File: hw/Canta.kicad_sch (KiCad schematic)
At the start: 41 parts, among them J1 USB_C_Receptacle_PowerOnly_6P, J101 Conn_01x01, J102 Conn_01x01, J103 Conn_01x01, J104 Conn_01x01, J105 Conn_01x01, J106 Conn_01x01, J107 Conn_01x01, J108 Conn_01x01, J109 Conn_01x01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

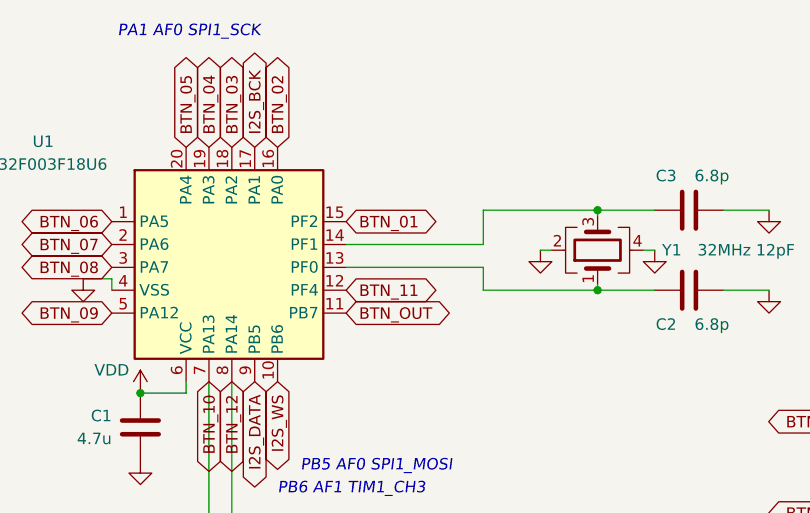
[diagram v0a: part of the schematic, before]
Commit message: Revise pin assignment; submit for fab (Rev. 2)
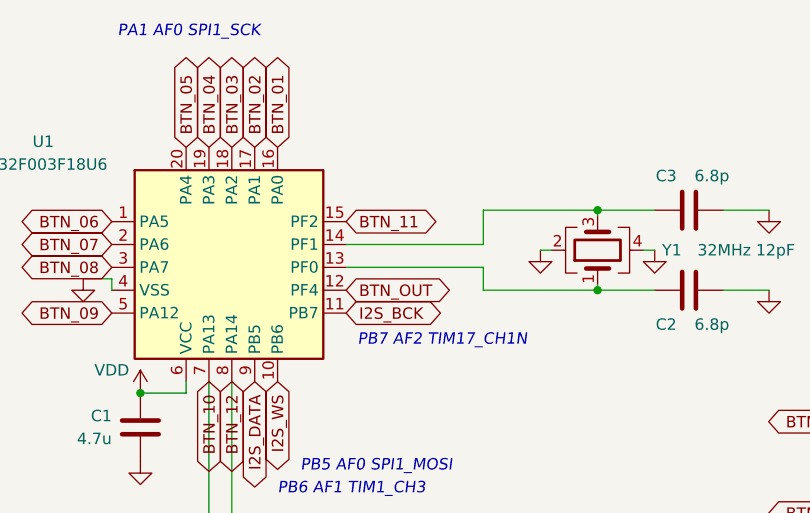
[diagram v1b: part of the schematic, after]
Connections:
- net BTN_01: now also U1.16 (PA0); no longer U1.15 (PF2)
- net BTN_02: now also U1.17 (PA1); no longer U1.16 (PA0)
- net BTN_11: now also U1.15 (PF2); no longer U1.12 (PF4)
- net BTN_OUT: now also U1.12 (PF4); no longer U1.11 (PB7)
- net I2S_BCK: now also U1.11 (PB7); no longer U1.17 (PA1)
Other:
- note added: "PB7 AF2 TIM17_CH1N"

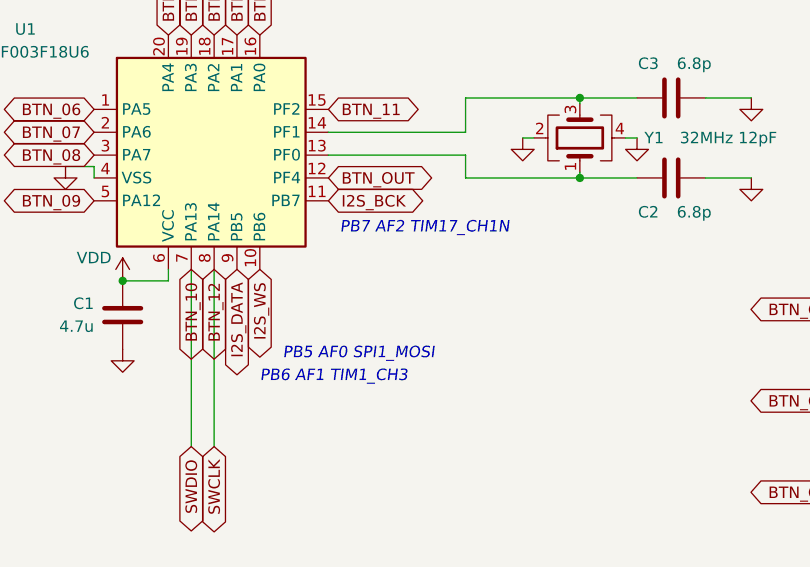
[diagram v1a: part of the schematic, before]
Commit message: Improve signal timings
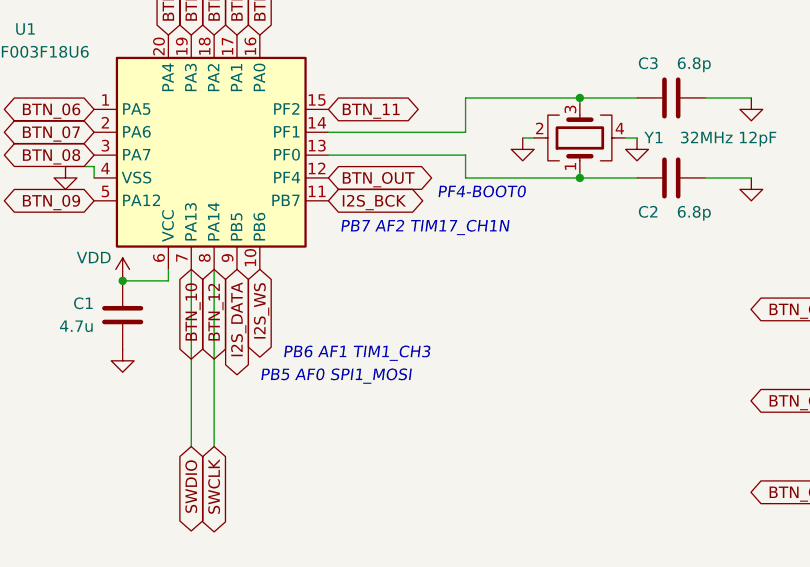
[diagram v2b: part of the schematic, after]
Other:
- note added: "PF4-BOOT0"
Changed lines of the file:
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@@
     (stroke (width 0) (type default))
   )
-  (text "PB5 AF0 SPI1_MOSI" (at 169.545 67.31 0)
+  (text "PB5 AF0 SPI1_MOSI" (at 167.005 69.85 0)
+    (effects (font (size 1.27 1.27) italic) (justify left bottom))
+  )
+  (text "PF4-BOOT0" (at 186.69 49.53 0)
     (effects (font (size 1.27 1.27) italic) (justify left bottom))
   )
@@
     (effects (font (size 1.27 1.27) italic) (justify right bottom))
   )
-  (text "PB6 AF1 TIM1_CH3" (at 167.005 69.85 0)
+  (text "PB6 AF1 TIM1_CH3" (at 169.545 67.31 0)
     (effects (font (size 1.27 1.27) italic) (justify left bottom))
   )
